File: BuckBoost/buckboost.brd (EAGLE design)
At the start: 100.1 x 80.4 mm, 13 parts

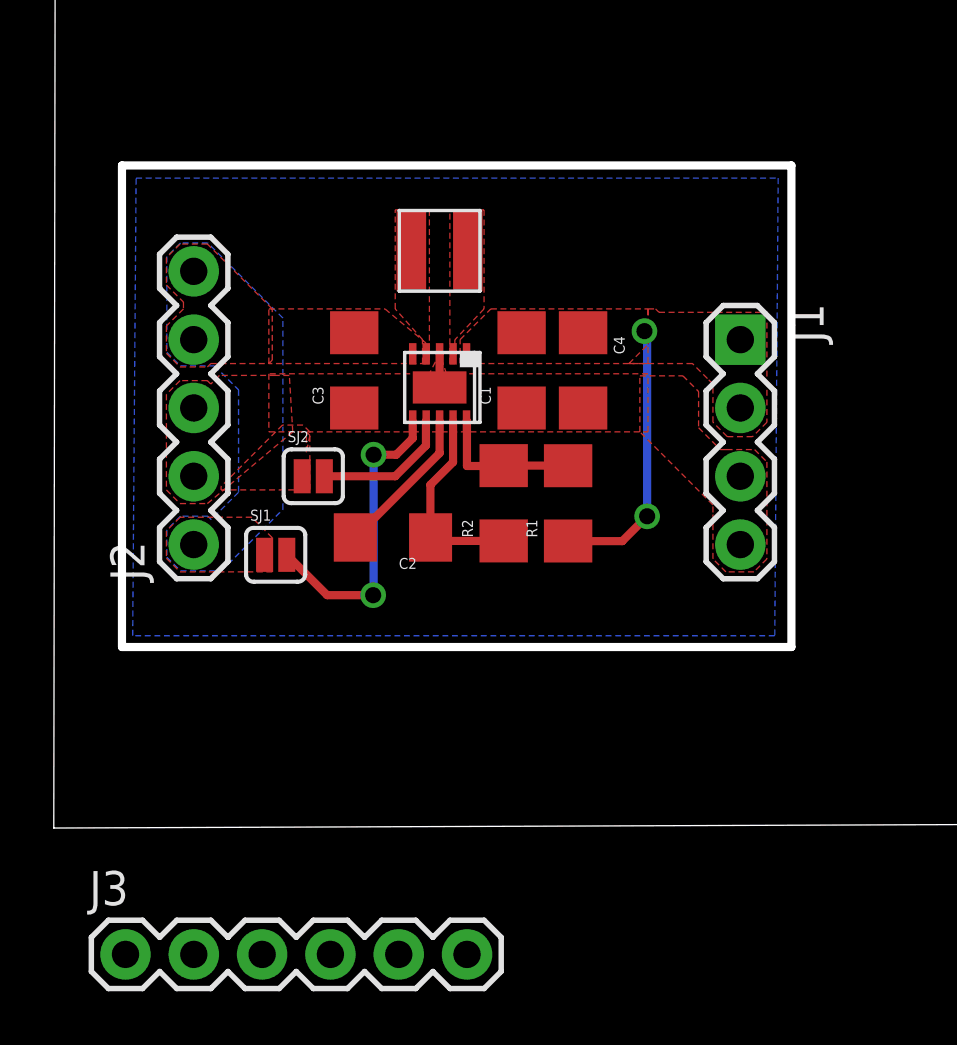
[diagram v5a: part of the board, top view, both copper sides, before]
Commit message: integrated 6 pin header
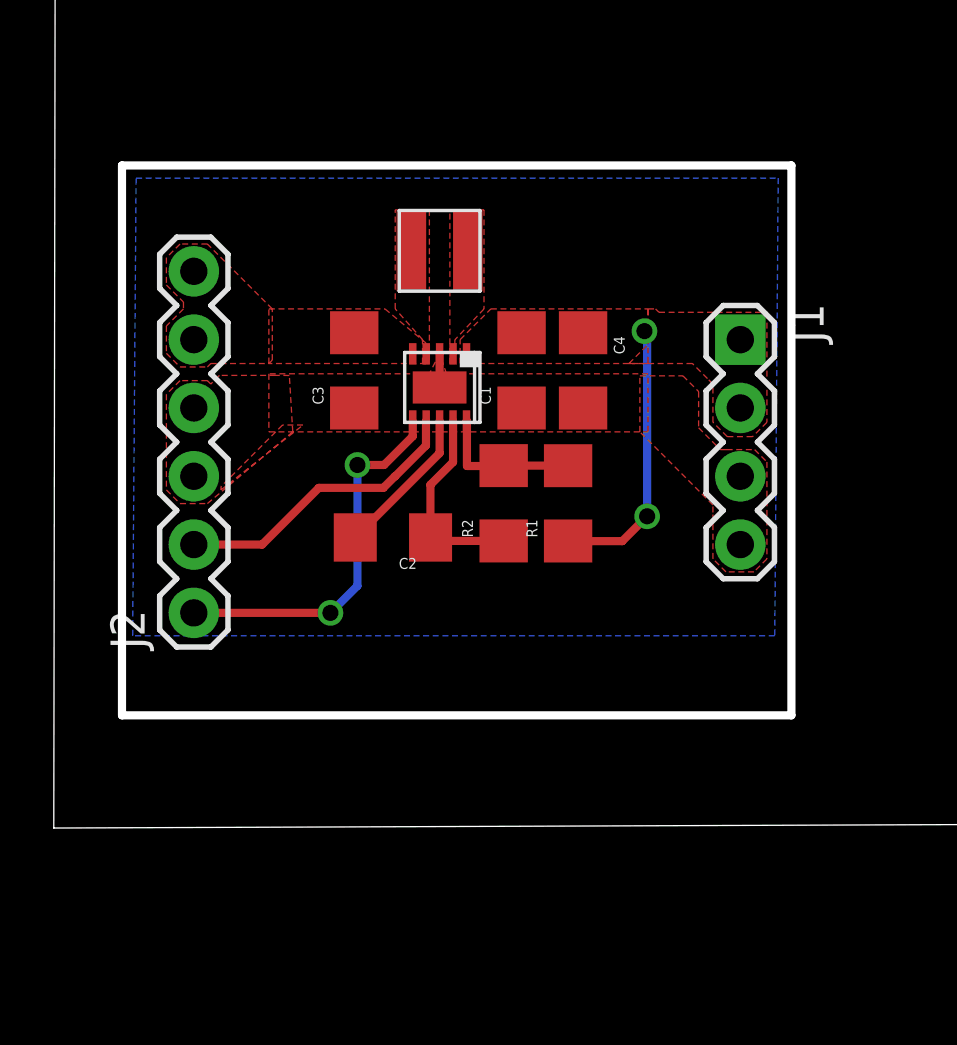
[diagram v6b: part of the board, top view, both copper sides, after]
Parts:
- removed J3: (no value), SparkFun-Connectors:1X06
- removed SJ1, SJ2: SOLDERJUMPERNC, SparkFun-Retired:SJ_2S
- J2: device SparkFun-Connectors:1X05 -> SparkFun-Connectors:1X06
- moved J2 2.54 mm to (5.08, 7.62)
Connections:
- net GND: now also J2.4; no longer J2.2, SJ2.1
- net N$2: now also J2.1; no longer SJ1.2
- net N$4: now also J2.2; no longer SJ2.2
- net VIN: now also J2.6; no longer J2.1, J2.4, SJ1.1
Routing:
- net N$4: track 5.16 -> 11.1 mm
- net N$2: track 11.4 -> 14.1 mm
- removed copper zone on layer 16, net VIN
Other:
- outline, holes or cut-outs redrawn
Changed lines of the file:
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@@
 <wire x1="0" y1="80" x2="-0.127" y2="-0.381" width="0" layer="20"/>
 <wire x1="2.40935625" y1="24.257" x2="27.30135625" y2="24.257" width="0.3048" layer="20"/>
-<wire x1="27.30135625" y1="24.257" x2="27.30135625" y2="6.35" width="0.3048" layer="20"/>
-<wire x1="27.30135625" y1="6.35" x2="2.40935625" y2="6.35" width="0.3048" layer="20"/>
-<wire x1="2.40935625" y1="6.35" x2="2.40935625" y2="24.257" width="0.3048" layer="20"/>
+<wire x1="27.30135625" y1="24.257" x2="27.30135625" y2="3.81" width="0.3048" layer="20"/>
+<wire x1="27.30135625" y1="3.81" x2="2.40935625" y2="3.81" width="0.3048" layer="20"/>
+<wire x1="2.40935625" y1="3.81" x2="2.40935625" y2="24.257" width="0.3048" layer="20"/>
 </plain>
 <attributes>
@@
 <attribute name="PROD_ID" value="CONN-09696" x="25.401459375" y="17.779471875" size="1.778" layer="27" rot="R270" display="off"/>
 </element>
-<element name="J2" library="SparkFun-Connectors" package="1X05" value="" x="5.07635625" y="10.16" rot="R90"/>
-<element name="SJ1" library="SparkFun-Retired" package="SJ_2S" value="SOLDERJUMPERNC" x="8.12435625" y="9.779"/>
-<element name="SJ2" library="SparkFun-Retired" package="SJ_2S" value="SOLDERJUMPERNC" x="9.52135625" y="12.7"/>
-<element name="J3" library="SparkFun-Connectors" package="1X06" value="" x="2.54" y="-5.08">
-<attribute name="PROD_ID" value="CONN-08437" x="2.54" y="-5.08" size="1.778" layer="27" display="off"/>
+<element name="J2" library="SparkFun-Connectors" package="1X06" value="" x="5.08" y="7.62" rot="R90">
+<attribute name="PROD_ID" value="CONN-08437" x="5.08" y="7.62" size="1.778" layer="27" rot="R90" display="off"/>
 </element>
 </elements>
@@
 <vertex x="13.71235625" y="17.653"/>
 </polygon>
-<contactref element="J2" pad="5"/>
-<contactref element="J2" pad="4"/>
 <polygon width="0.3048" layer="1" thermals="no" rank="2">
 <vertex x="7.99735625" y="18.923"/>
@@
 <vertex x="7.99735625" y="17.018"/>
 </polygon>
-<polygon width="0.3048" layer="16" thermals="no">
-<vertex x="4.5847" y="21.3741"/>
-<vertex x="4.0767" y="20.8661"/>
-<vertex x="4.0767" y="17.3101"/>
-<vertex x="4.5847" y="16.8021"/>
-<vertex x="5.8547" y="16.8021"/>
-<vertex x="6.7437" y="15.9131"/>
-<vertex x="6.7437" y="12.1031"/>
-<vertex x="5.7277" y="11.0871"/>
-<vertex x="5.6007" y="11.2141"/>
-<vertex x="4.5847" y="11.2141"/>
-<vertex x="4.0767" y="10.7061"/>
-<vertex x="4.0767" y="9.6901"/>
-<vertex x="4.5847" y="9.1821"/>
-<vertex x="6.1087" y="9.1821"/>
-<vertex x="8.3947" y="11.4681"/>
-<vertex x="8.3947" y="18.5801"/>
-<vertex x="5.6007" y="21.3741"/>
-</polygon>
-<contactref element="J2" pad="1"/>
-<contactref element="SJ1" pad="1"/>
-<polygon width="0.3048" layer="1" thermals="no" rank="2">
-<vertex x="7.23535625" y="11.176"/>
-<vertex x="4.56835625" y="11.176"/>
-<vertex x="4.06035625" y="10.668"/>
-<vertex x="4.06035625" y="9.652"/>
-<vertex x="4.56835625" y="9.144"/>
-<vertex x="7.99735625" y="9.144"/>
-<vertex x="7.99735625" y="10.414"/>
-</polygon>
+<contactref element="J2" pad="6"/>
+<contactref element="J2" pad="5"/>
 </signal>
 <signal name="N$3">
@@
 <vertex x="2.8067" y="6.7691"/>
 </polygon>
-<contactref element="J2" pad="3"/>
-<contactref element="J2" pad="2"/>
 <polygon width="0.3048" layer="1" thermals="no" rank="3">
 <vertex x="4.56835625" y="16.256"/>
@@
 <vertex x="5.58435625" y="16.256"/>
 </polygon>
-<contactref element="SJ2" pad="1"/>
 <polygon width="0.3048" layer="1" thermals="no" rank="3">
 <vertex x="6.09235625" y="12.192"/>
-<vertex x="9.39435625" y="12.192"/>
-<vertex x="9.39435625" y="14.351"/>
 <vertex x="9.14035625" y="14.605"/>
 <vertex x="8.37835625" y="14.605"/>
 <vertex x="6.09235625" y="12.319"/>
-</polygon>
-<polygon width="0.3048" layer="1" thermals="no" rank="3">
-<vertex x="9.26735625" y="13.589"/>
-<vertex x="9.26735625" y="14.351"/>
-<vertex x="9.39435625" y="14.224"/>
 </polygon>
 <contactref element="J1" pad="3"/>
@@
 <vertex x="24.8666" y="13.6906"/>
 </polygon>
+<contactref element="J2" pad="4"/>
+<contactref element="J2" pad="3"/>
 </signal>
 <signal name="L1">
@@
 <signal name="N$2">
 <contactref element="U$1" pad="6"/>
-<contactref element="SJ1" pad="2"/>
-<wire x1="13.22035625" y1="14.752" x2="13.22035625" y2="14.113" width="0.3048" layer="1"/>
-<via x="11.764178125" y="13.500103125" extent="1-16" drill="0.6" shape="square"/>
-<via x="11.748934375" y="8.277859375" extent="1-16" drill="0.6" shape="square"/>
-<wire x1="11.764178125" y1="13.500103125" x2="11.764178125" y2="8.293103125" width="0.3048" layer="16"/>
-<wire x1="11.764178125" y1="8.293103125" x2="11.748934375" y2="8.277859375" width="0.3048" layer="16"/>
-<wire x1="13.22035625" y1="14.113" x2="12.607459375" y2="13.500103125" width="0.3048" layer="1"/>
-<wire x1="12.607459375" y1="13.500103125" x2="11.764178125" y2="13.500103125" width="0.3048" layer="1"/>
-<wire x1="11.748934375" y1="8.277859375" x2="10.037396875" y2="8.277859375" width="0.3048" layer="1"/>
-<wire x1="10.037396875" y1="8.277859375" x2="8.53625625" y2="9.779" width="0.3048" layer="1"/>
+<contactref element="J2" pad="1"/>
+<wire x1="13.22035625" y1="14.752" x2="13.22035625" y2="14.18555625" width="0.3048" layer="1"/>
+<wire x1="13.22035625" y1="14.18555625" x2="12.1539" y2="13.1191" width="0.3048" layer="1"/>
+<wire x1="12.1539" y1="13.1191" x2="11.1633" y2="13.1191" width="0.3048" layer="1"/>
+<via x="11.1633" y="13.1191" extent="1-16" drill="0.6" shape="square"/>
+<wire x1="11.1633" y1="13.1191" x2="11.1633" y2="8.6233" width="0.3048" layer="16"/>
+<wire x1="11.1633" y1="8.6233" x2="10.16" y2="7.62" width="0.3048" layer="16"/>
+<via x="10.16" y="7.62" extent="1-16" drill="0.6" shape="square"/>
+<wire x1="10.16" y1="7.62" x2="5.08" y2="7.62" width="0.3048" layer="1"/>
 </signal>
 <signal name="N$4">
 <contactref element="U$1" pad="7"/>
-<contactref element="SJ2" pad="2"/>
-<wire x1="9.93325625" y1="12.7" x2="12.56935625" y2="12.7" width="0.3048" layer="1"/>
 <wire x1="12.56935625" y1="12.7" x2="13.71235625" y2="13.843" width="0.3048" layer="1"/>
 <wire x1="13.71235625" y1="13.843" x2="13.71235625" y2="14.744" width="0.3048" layer="1"/>
 <wire x1="13.71235625" y1="14.744" x2="13.72035625" y2="14.752" width="0.3048" layer="1"/>
+<contactref element="J2" pad="2"/>
+<wire x1="5.08" y1="10.16" x2="7.62" y2="10.16" width="0.3048" layer="1"/>
+<wire x1="12.56935625" y1="12.7" x2="12.5603" y2="12.7" width="0.3048" layer="1"/>
+<wire x1="12.5603" y1="12.7" x2="12.1285" y2="12.2682" width="0.3048" layer="1"/>
+<wire x1="12.1285" y1="12.2682" x2="9.7282" y2="12.2682" width="0.3048" layer="1"/>
+<wire x1="9.7282" y1="12.2682" x2="7.62" y2="10.16" width="0.3048" layer="1"/>
 </signal>
 </signals>
